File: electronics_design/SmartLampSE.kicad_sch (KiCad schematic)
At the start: 15 parts, among them J1 Screw_Terminal_01x02, M1 PIC16F886-IP, U1 L7805, Y1 Crystal

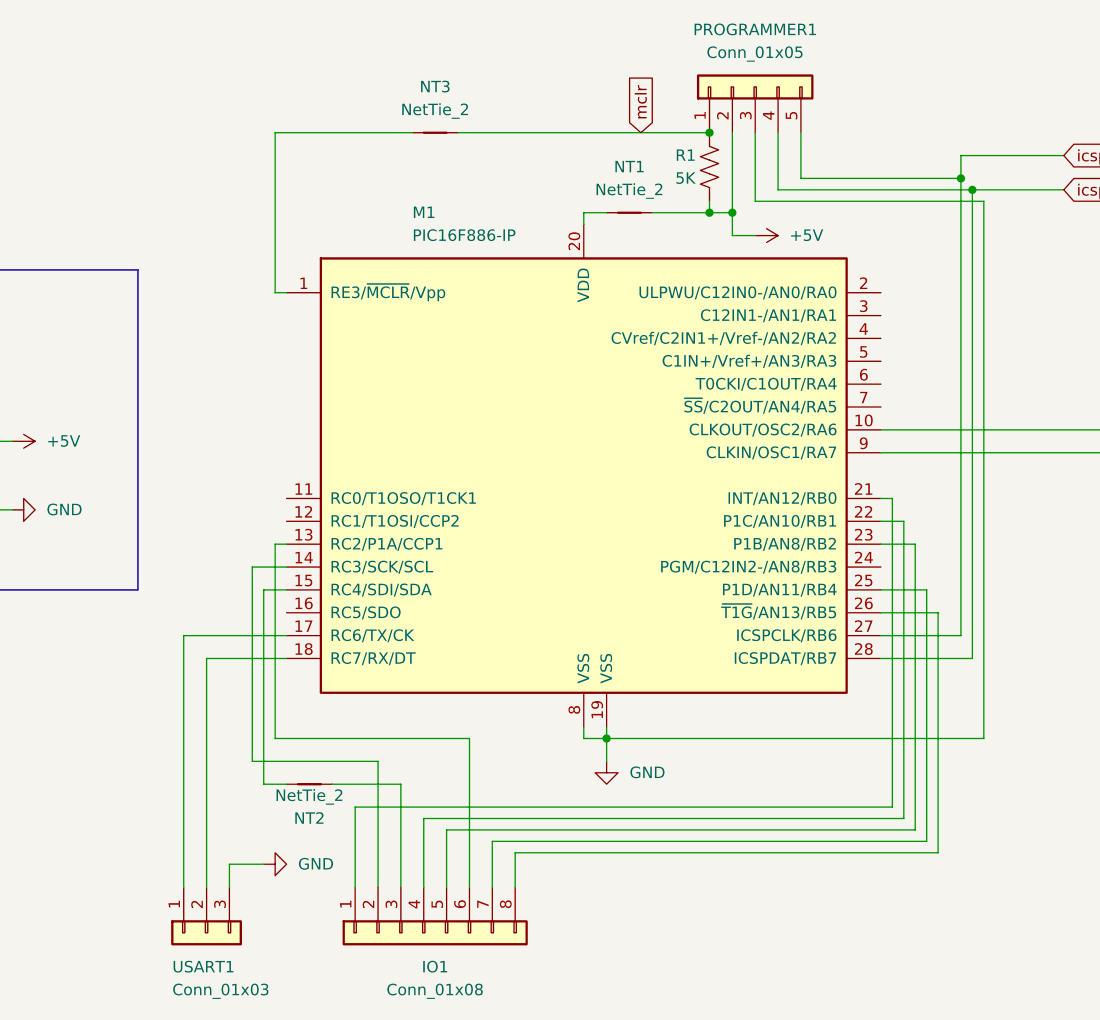
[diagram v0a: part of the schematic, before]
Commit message: Separate board IO interface
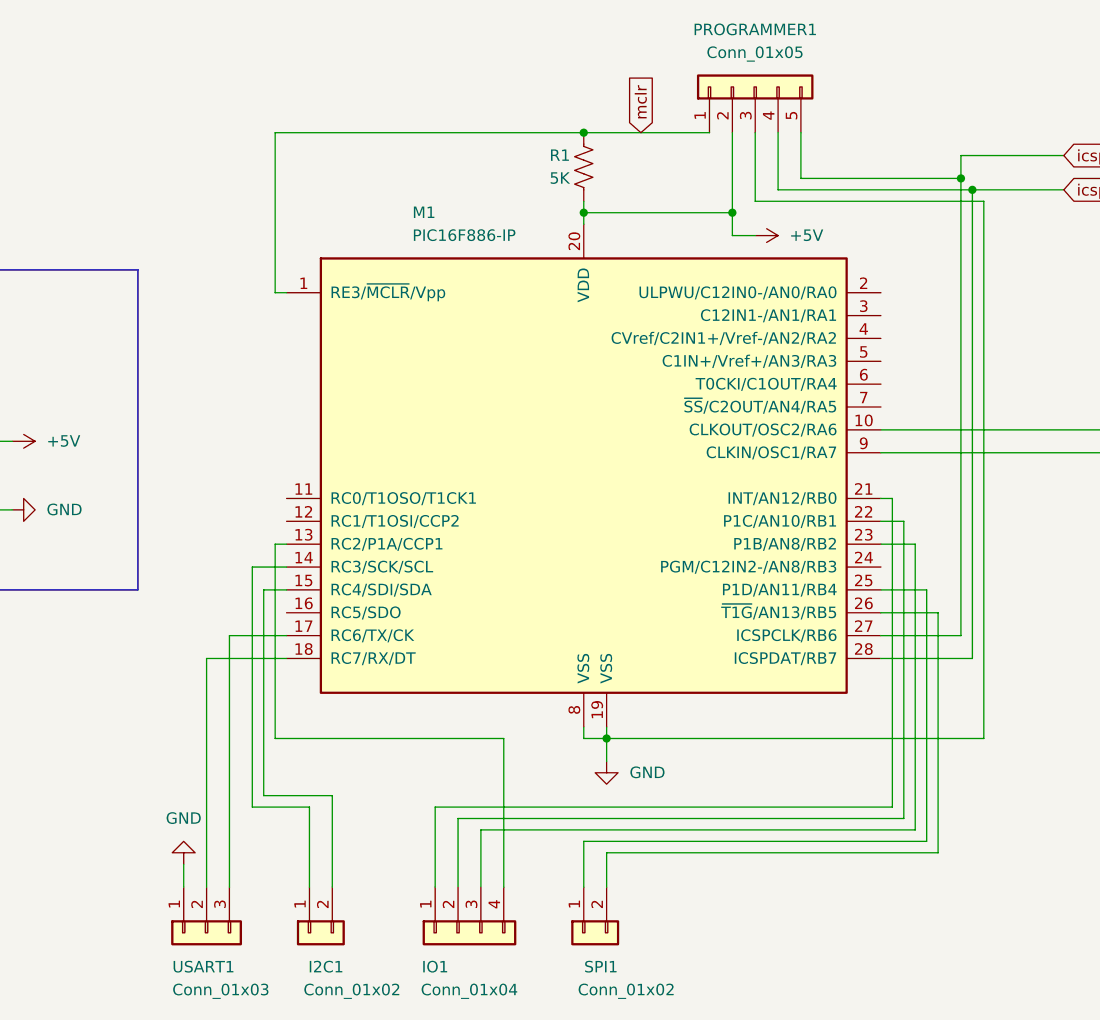
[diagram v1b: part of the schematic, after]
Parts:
- removed IO1: Conn_01x08, Connector_PinSocket_2.54mm:PinSocket_1x08_P2.54mm_Vertical, symbol Connector_Generic:Conn_01x08
- removed NT1, NT3: NetTie_2, Custom_Library:NetTie-2_THT_Custom_Pad1.0mm, symbol Device:NetTie_2
- removed NT2: NetTie_2, NetTie:NetTie-2_THT_Pad1.0mm, symbol Device:NetTie_2
- added I2C1, SPI1: Conn_01x02, Connector_PinSocket_2.54mm:PinSocket_1x02_P2.54mm_Vertical, symbol Connector_Generic:Conn_01x02
- added IO1: Conn_01x04, Connector_PinSocket_2.54mm:PinSocket_1x04_P2.54mm_Vertical, symbol Connector_Generic:Conn_01x04
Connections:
- net +5V: now also M1.20 (VDD)
- net GND: now also USART1.1 (Pin_1); no longer USART1.3 (Pin_3)
- net mclr: now also M1.1 (RE3/~{MCLR}/Vpp)
- net at M1.17 (RC6/TX/CK): now also USART1.3 (Pin_3); no longer USART1.1 (Pin_1)
- net at M1.15 (RC4/SDI/SDA): now also I2C1.2 (Pin_2)
- net at M1.13 (RC2/P1A/CCP1): now also IO1.4 (Pin_4)
- net at M1.14 (RC3/SCK/SCL): now also I2C1.1 (Pin_1)
- net at M1.21 (INT/AN12/RB0): now also IO1.1 (Pin_1)
- net at M1.22 (P1C/AN10/RB1): now also IO1.2 (Pin_2)
- net at M1.23 (P1B/AN8/RB2): now also IO1.3 (Pin_3)
- net at M1.25 (P1D/AN11/RB4): now also SPI1.1 (Pin_1)
- net at M1.26 (~{T1G}/AN13/RB5): now also SPI1.2 (Pin_2)
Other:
- moved on the sheet: R1

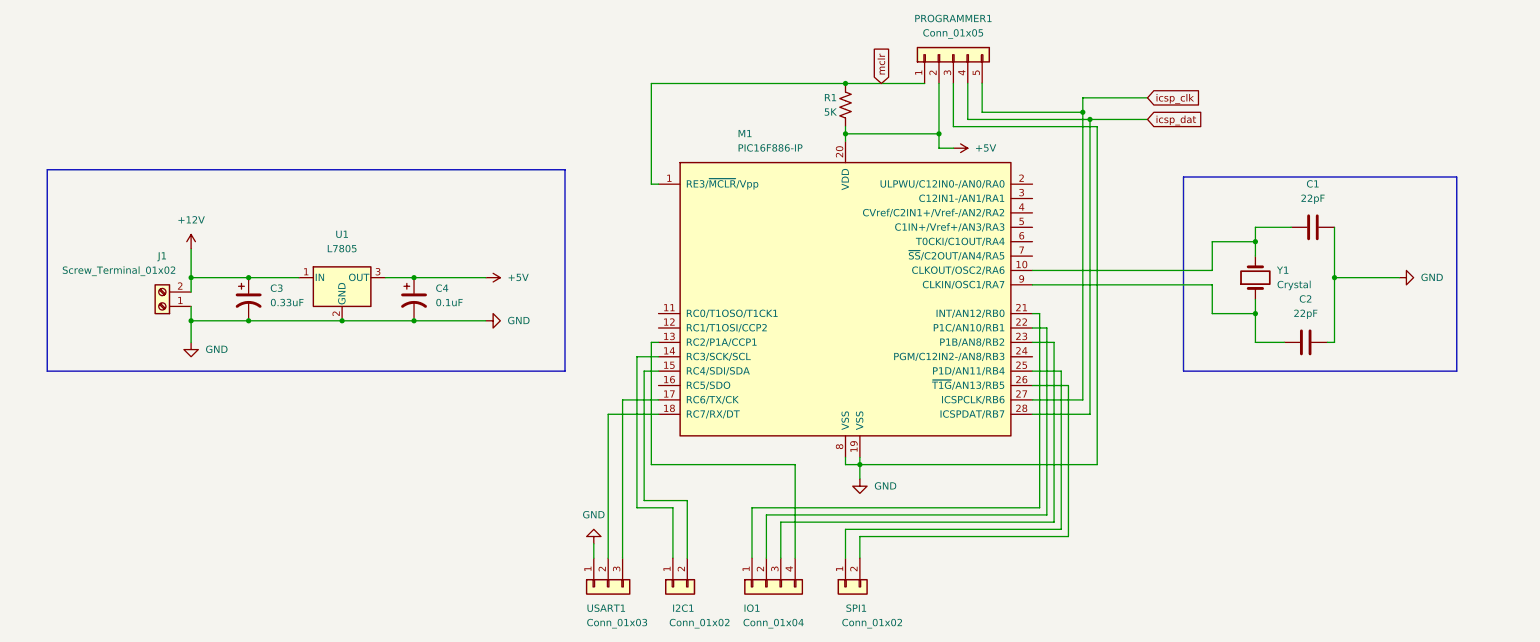
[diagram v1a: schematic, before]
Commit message: Separate board IO interface
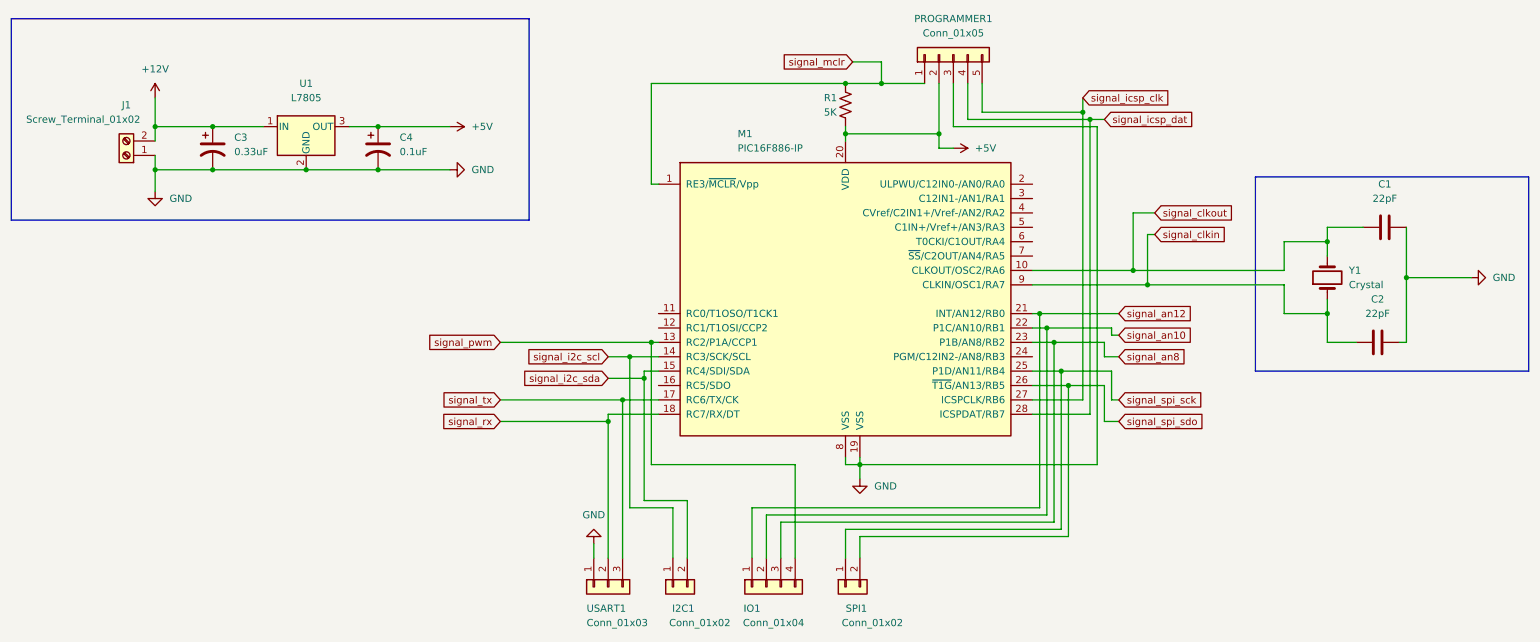
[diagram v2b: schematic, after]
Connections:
- net signal_rx: now reaches M1.18 (RC7/RX/DT), USART1.2 (Pin_2)
- net signal_tx: now reaches M1.17 (RC6/TX/CK), USART1.3 (Pin_3)
- net signal_clkout: now reaches C1.1, M1.10 (CLKOUT/OSC2/RA6), Y1.2
- net signal_i2c_scl: now reaches I2C1.1 (Pin_1), M1.14 (RC3/SCK/SCL)
- net signal_i2c_sda: now reaches I2C1.2 (Pin_2), M1.15 (RC4/SDI/SDA)
- net signal_pwm: now reaches IO1.4 (Pin_4), M1.13 (RC2/P1A/CCP1)
- net signal_an12: now reaches IO1.1 (Pin_1), M1.21 (INT/AN12/RB0)
- net signal_an10: now reaches IO1.2 (Pin_2), M1.22 (P1C/AN10/RB1)
- net signal_an8: now reaches IO1.3 (Pin_3), M1.23 (P1B/AN8/RB2)
- net signal_spi_sck: now reaches M1.25 (P1D/AN11/RB4), SPI1.1 (Pin_1)
- net signal_spi_sdo: now reaches M1.26 (~{T1G}/AN13/RB5), SPI1.2 (Pin_2)
- net signal_clkin: now reaches C2.1, M1.9 (CLKIN/OSC1/RA7), Y1.1
- net icsp_clk renamed signal_icsp_clk
- net icsp_dat renamed signal_icsp_dat
- net mclr renamed signal_mclr
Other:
- moved on the sheet: C1, C2, C3, C4, J1, U1, Y1
